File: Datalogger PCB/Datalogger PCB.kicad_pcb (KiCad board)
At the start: 4 copper layers, 42.2 x 104 mm, 53 parts, among them J1 Conn_01x02_Pin, M1 Motor_Servo, M2 Motor_Servo, M3 Motor_Servo, M4 Motor_Servo, Q1 IRLB8721PBF, Q2 IRLB8721PBF, Q3 IRLB8721PBF, Q4 IRLB8721PBF, U1 LPS25HB, U2 Teensy4.1, U3 BNO055, U5 NRF24L01_Breakout, U6 AZ1117-5.0

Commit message: V2 of the PCB
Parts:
- removed PYRO1, PYRO2, PYRO3, PYRO4: Conn_01x02_Pin, Connector_PinHeader_1.27mm:PinHeader_1x02_P1.27mm_Vertical
- removed Q1, Q2, Q3, Q4: IRLB8721PBF, Package_TO_SOT_THT:TO-220-3_Vertical
- removed R14, R15, R16, R17: 10k, Resistor_SMD:R_0603_1608Metric_Pad0.98x0.95mm_HandSolder
- added PYRO_1-2: Screw_Terminal_01x04, TerminalBlock:TerminalBlock_bornier-4_P5.08mm, F.Cu at (141.4, 63.1)
- added PYRO_3-4: Screw_Terminal_01x04, TerminalBlock:TerminalBlock_bornier-4_P5.08mm, F.Cu at (175.9, 77.8)
- added U4: AMS1117-5.0, Package_TO_SOT_SMD:SOT-223-3_TabPin2, B.Cu at (145.7, 135.5)
- added U7: VN5E160STR-E, SOIC127P600X175-8N:SOIC127P600X175-8N, B.Cu at (147.1, 75.8)
- added U8: VN5E160STR-E, SOIC127P600X175-8N:SOIC127P600X175-8N, B.Cu at (170.3, 75.2)
- added U9: VN5E160STR-E, SOIC127P600X175-8N:SOIC127P600X175-8N, B.Cu at (170.2, 65.1)
- U6: value AZ1117-5.0 -> VN5E160STR-E; footprint Package_TO_SOT_SMD:SOT-223 -> SOIC127P600X175-8N:SOIC127P600X175-8N
- moved U6 69.8 mm to (147.1, 65.7), turned to 180 degrees
- moved M4 7.41 mm to (171.5, 49.0), turned to 90 degrees
- moved M3 7.41 mm to (171.5, 55.4), turned to 90 degrees
- moved H1 2.16 mm to (140.0, 44.7)
- moved H2 2.16 mm to (177.2, 44.7)
- turned R13 to 90 degrees
- renumbered U2 to U1, U3 to U2, U1 to U3
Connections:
- R13 pad 1: GND -> /BATT_VOLTAGE
- R13 pad 2: /BATT_VOLTAGE -> GND
- R7 pad 1: Net-(U2-15_A1_RX3_SPDIF_IN) -> Net-(U1-17_A3_TX4_SDA1)
- U1 pad 16: unconnected-(U2-24_A10_TX6_SCL2-Pad16) -> /PYRO_4_STATUS
- U1 pad 17: unconnected-(U2-25_A11_RX6_SDA2-Pad17) -> /PYRO_4
- U1 pad 18: /PYRO_3 -> /PYRO_3_STATUS
- U1 pad 19: /PYRO_4 -> /PYRO_3
- U1 pad 20: /SERVO_4 -> /SERVO_3
- U1 pad 21: /SERVO_3 -> /SERVO_4
- U1 pad 32: /PYRO_2 -> /PYRO_1_STATUS
- U1 pad 36: /ERASE_BTN -> /PYRO_2
- U1 pad 37: Net-(U2-15_A1_RX3_SPDIF_IN) -> /PYRO_2_STATUS
- U1 pad 38: unconnected-(U2-16_A2_RX4_SCL1-Pad38) -> /ERASE_BTN
- U1 pad 39: unconnected-(U2-17_A3_TX4_SDA1-Pad39) -> Net-(U1-17_A3_TX4_SDA1)
- U6 pad 2: +5V -> /PYRO_1
- U6 pad 3: /VIN -> /PYRO_1_STATUS
- U6 pad 4: (no net) -> unconnected-(U6-STAT_DIS-Pad4)
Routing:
- net /PYRO_4_STATUS: track 0.00 -> 43.5 mm, vias 0 -> 1
- net /PYRO_2_STATUS: track 0.00 -> 40.3 mm
- net /PYRO_1_STATUS: track 0.00 -> 37.8 mm
- net /PYRO_3_STATUS: track 0.00 -> 27.5 mm, vias 0 -> 1
- net /PYRO_3: track 45.8 -> 23.2 mm
- net /VIN: track 143.9 -> 161.3 mm, vias 1 -> 5
- net GND: track 73.3 -> 56.6 mm, vias 7 -> 11
- net +5V: track 146.1 -> 157.9 mm, vias 2 -> 3
- net /PYRO_1: track 46.6 -> 36.5 mm
- net /PYRO_4: track 30.5 -> 39.3 mm
- net Net-(PYRO_1-2-Pin_3): track 0.00 -> 7.12 mm
- net Net-(PYRO_3-4-Pin_3): track 0.00 -> 6.72 mm
- net Net-(PYRO_1-2-Pin_1): track 0.00 -> 6.65 mm
- net Net-(PYRO1-Pin_2): track 6.50 -> 0.00 mm
- net Net-(PYRO4-Pin_2): track 6.50 -> 0.00 mm
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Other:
- board size 42.2 x 104 mm -> 42.2 x 101.8 mm
- board text added: "CH 1"
- board text added: "CH 2"
- board text added: "CH 3"
- board text added: "CH 4"
- board text added: "Signal + -"

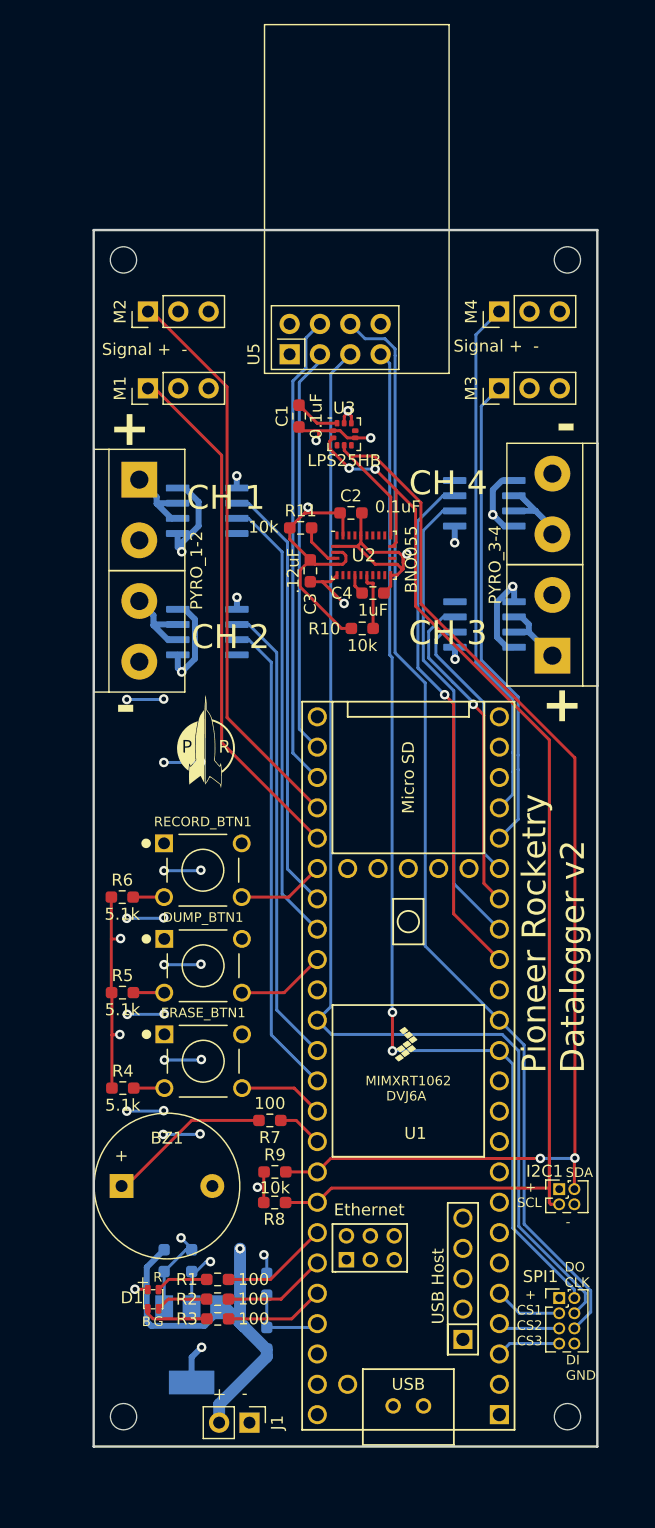
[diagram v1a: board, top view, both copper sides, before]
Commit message: Coverted to 2 layer board
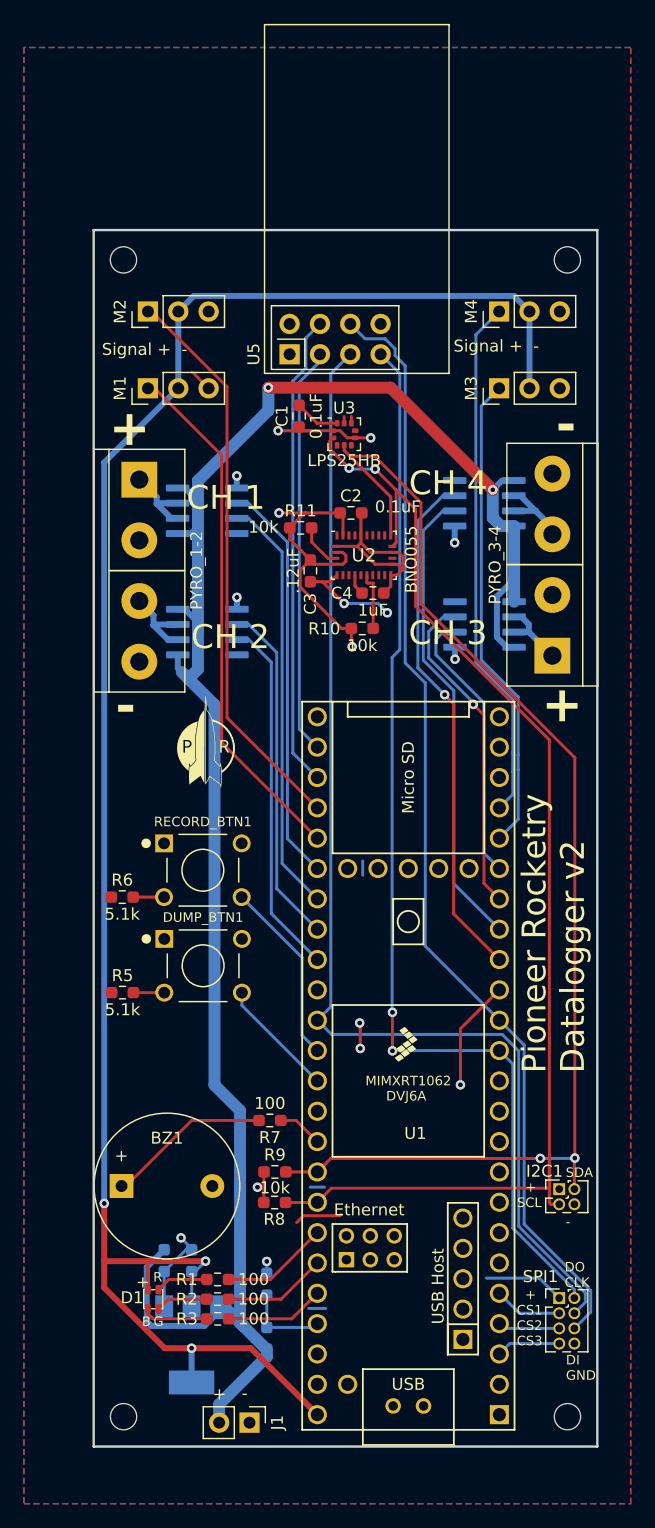
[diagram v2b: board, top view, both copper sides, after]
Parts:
- removed ERASE_BTN1: FSM8JH, Push Button:SW_FSM8JH
- removed R4: 5.1k, Resistor_SMD:R_0603_1608Metric_Pad0.98x0.95mm_HandSolder
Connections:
- U1 pad 30: /RECORD_BTN -> /PYRO_1
- U1 pad 31: /PYRO_1 -> /PYRO_1_STATUS
- U1 pad 32: /PYRO_1_STATUS -> /PYRO_2
- U1 pad 33: /DUMP_BTN -> /PYRO_2_STATUS
- U1 pad 36: /PYRO_2 -> /RECORD_BTN
- U1 pad 37: /PYRO_2_STATUS -> /DUMP_BTN
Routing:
- net /PYRO_2: track 39.0 -> 28.9 mm
- net /PYRO_2_STATUS: track 40.3 -> 30.1 mm
- net GND: track 56.6 -> 46.8 mm, vias 11 -> 8
- net /RECORD_BTN: track 7.32 -> 15.5 mm
- net /ERASE_BTN: track 7.11 -> 0.00 mm
- net +5V: track 157.9 -> 162.1 mm
- net Net-(ERASE_BTN1-Pad2): track 2.57 -> 0.00 mm
- net /DUMP_BTN: track 7.46 -> 10.0 mm
- net /PYRO_1: track 36.5 -> 34.0 mm
- net /PYRO_1_STATUS: track 37.8 -> 35.2 mm
- net /DO: track 91.0 -> 91.5 mm
- net +3.3V: track 61.6 -> 61.9 mm, vias 22 -> 8
- net /VIN: track 161.3 -> 161.4 mm, vias 5 -> 2
- added copper zone on B.Cu, net +3.3V
- added copper zone on F.Cu, net GND
- removed copper zone on In2.Cu, net +3.3V
- removed copper zone on In1.Cu, net GND
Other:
- copper layers 4 -> 2

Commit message: Change some trace widths, as well as spread out traces, and fixed silk screen issues
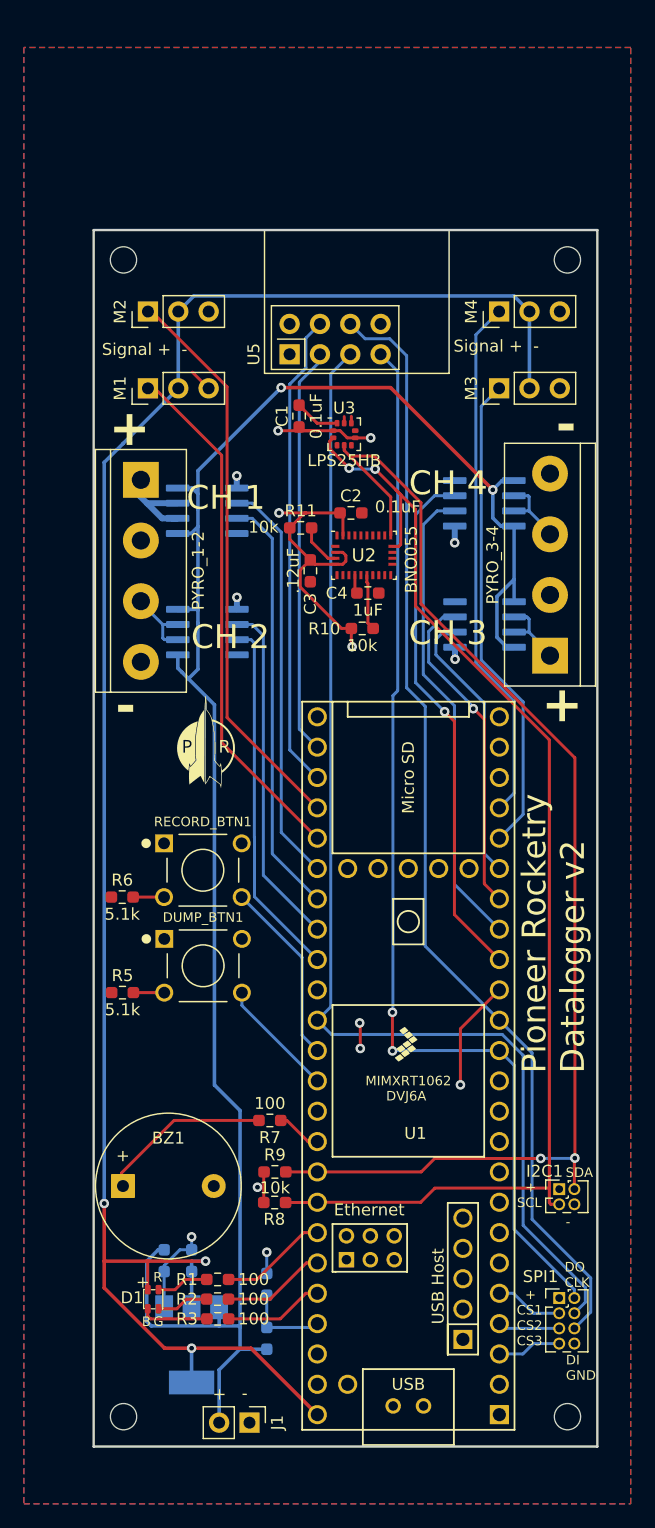
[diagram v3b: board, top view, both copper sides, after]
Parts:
- moved C4 0.43 mm to (160.5, 72.6)
- moved PYRO_3-4 0.20 mm to (175.8, 77.8)
- moved PYRO_1-2 0.13 mm to (141.5, 63.1)
- moved BZ1 0.12 mm to (140.0, 122.2)
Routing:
- net GND: track 46.8 -> 16.9 mm, vias 8 -> 6
- net +3.3V: track 61.9 -> 51.3 mm
- net Net-(PYRO_1-2-Pin_1): track 6.65 -> 8.41 mm
- net Net-(PYRO_1-2-Pin_3): track 7.12 -> 6.48 mm
- net Net-(BZ1--): track 13.8 -> 14.4 mm
- net /SCL: track 104.1 -> 104.7 mm
- net /PYRO_4_STATUS: track 43.5 -> 44.1 mm

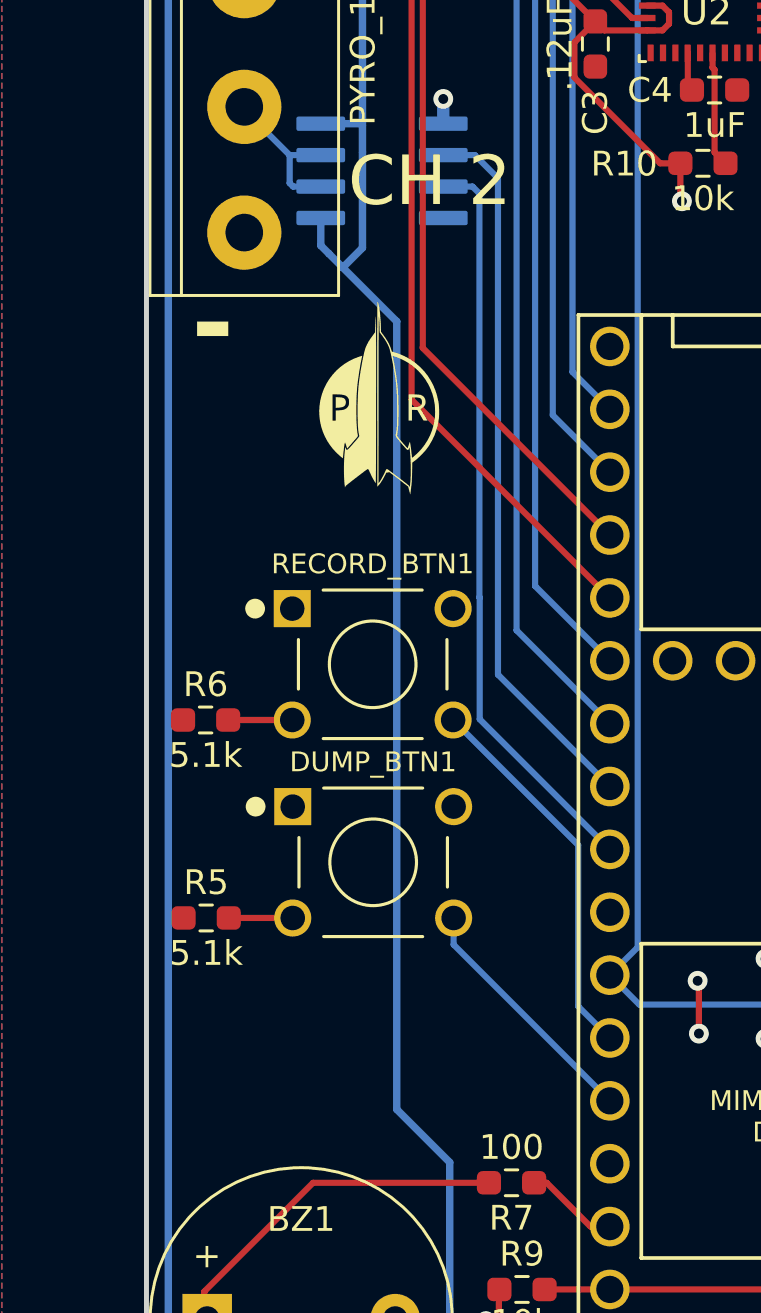
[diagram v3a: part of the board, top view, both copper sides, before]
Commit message: Added screw terminal for switching on/off pyro channels
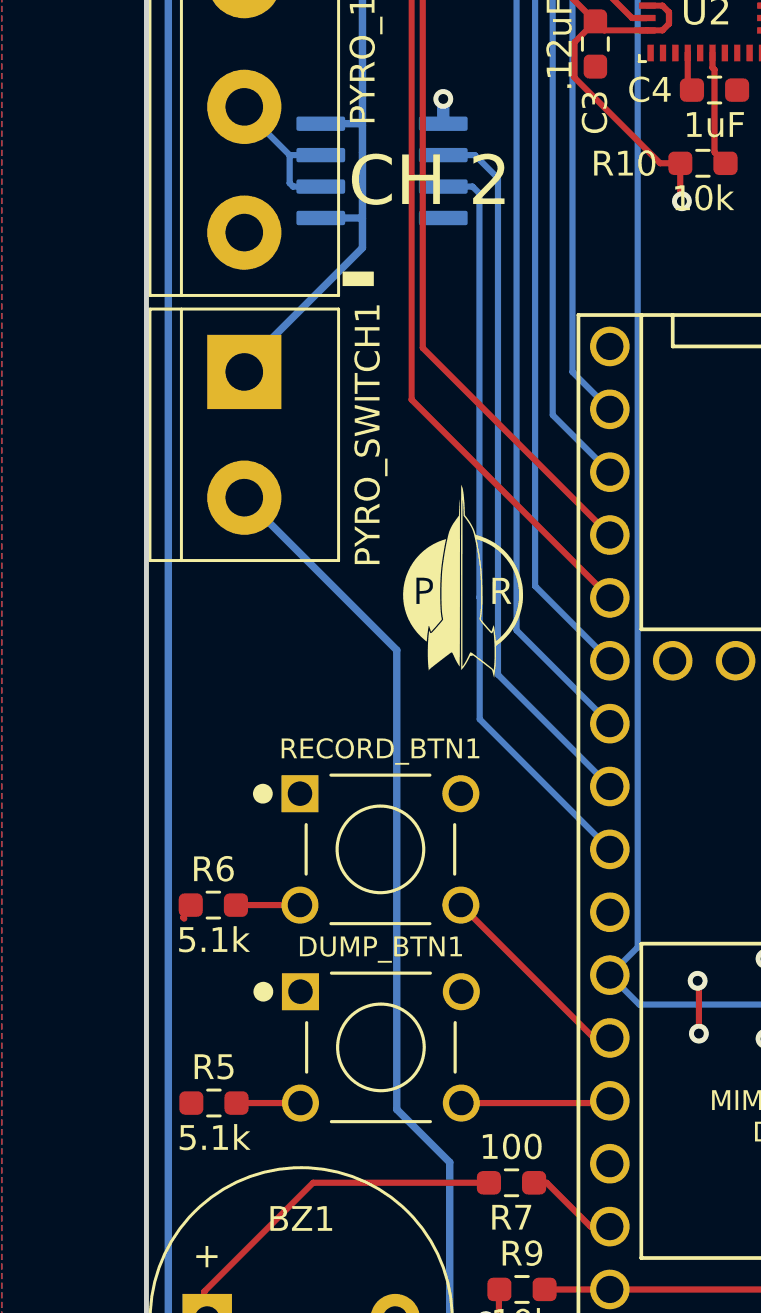
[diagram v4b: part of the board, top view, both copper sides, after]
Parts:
- added PYRO_SWITCH1: Screw_Terminal_01x02, TerminalBlock:TerminalBlock_bornier-2_P5.08mm, F.Cu at (141.5, 84.0)
- moved G*** 8.14 mm to (150.2, 92.2)
- moved DUMP_BTN1 7.48 mm to (147.0, 111.2)
- moved R5 7.48 mm to (140.3, 113.5)
- moved R6 7.48 mm to (140.2, 105.5)
- moved RECORD_BTN1 7.48 mm to (147.0, 103.2)
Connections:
- U6 pad 5: /VIN -> /PYRO_POWER
- U6 pad 8: /VIN -> /PYRO_POWER
- U7 pad 5: /VIN -> /PYRO_POWER
- U7 pad 8: /VIN -> /PYRO_POWER
- U8 pad 5: /VIN -> /PYRO_POWER
- U8 pad 8: /VIN -> /PYRO_POWER
- U9 pad 5: /VIN -> /PYRO_POWER
- U9 pad 8: /VIN -> /PYRO_POWER
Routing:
- net /VIN: track 161.4 -> 76.4 mm, vias 2 -> 0
- net /PYRO_POWER: track 0.00 -> 82.6 mm, vias 0 -> 2
- net /RECORD_BTN: track 15.5 -> 8.24 mm
- net /DUMP_BTN: track 10.0 -> 6.04 mm
